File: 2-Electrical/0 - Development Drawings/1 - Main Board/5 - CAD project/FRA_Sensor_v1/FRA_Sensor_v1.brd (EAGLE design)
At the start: 79 x 94 mm, 144 parts, among them IC1 CP2101, IC2 LMV611, J1 FTDI, J3 USB, T1 BC847, T2 BC847, T3 BC847, U1 DS1307Z, U2 ESP-WROOM-32, U3 CH340G, U4 W25Q32FV, U6 MMA8452QL, Y1 12MHz, Y2 32.768kHz, Y3 32.768kHz, Y4 12MHz

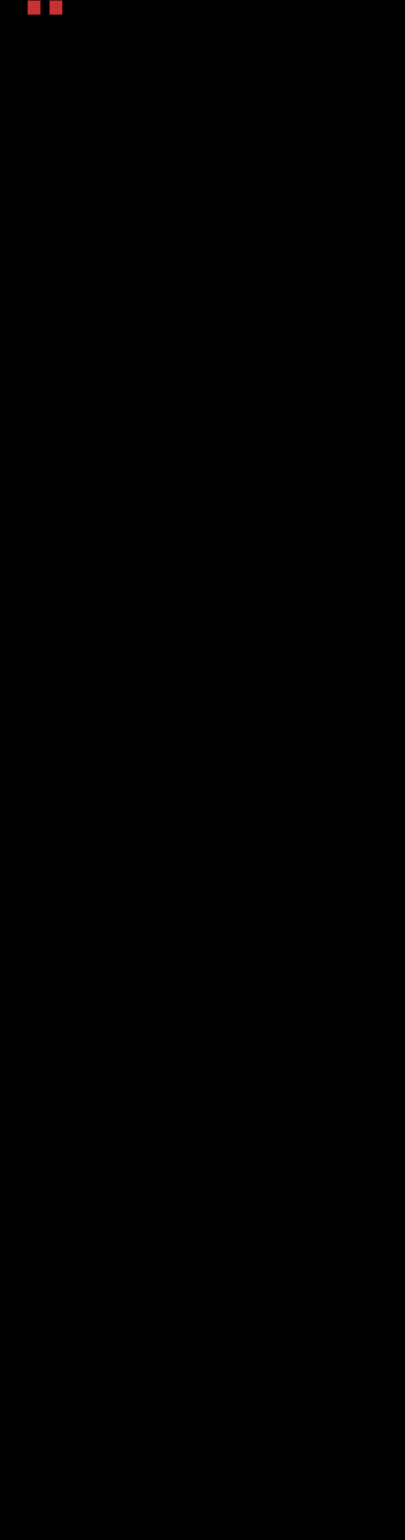
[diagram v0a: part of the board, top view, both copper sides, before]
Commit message: TGS2611 integration
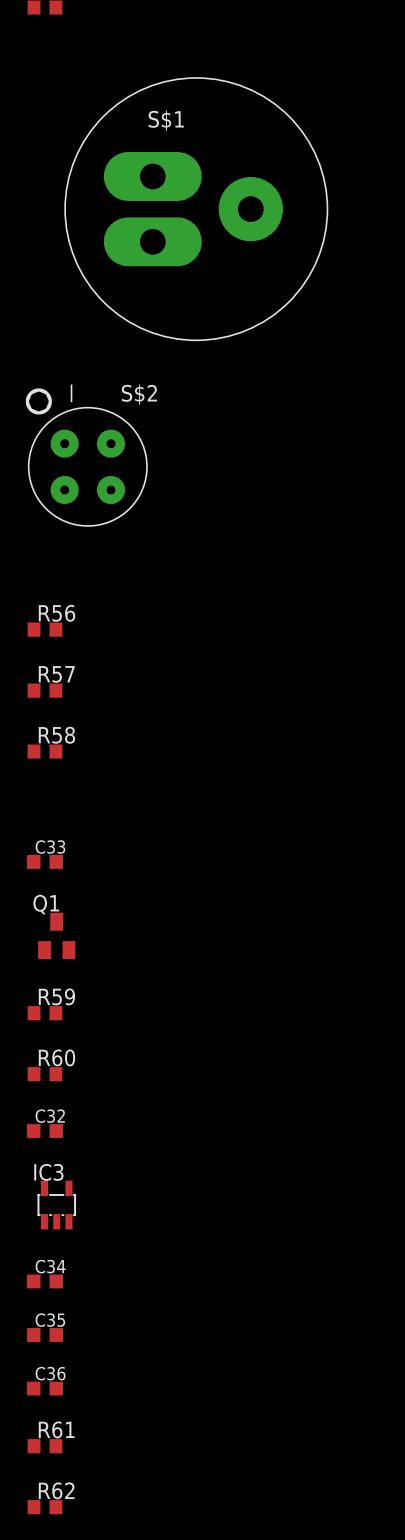
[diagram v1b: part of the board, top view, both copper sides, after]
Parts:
- added C32, C33, C34: 100n, resistor:C0603K
- added C35, C36: 1u, resistor:C0603K
- added IC3: TS520533, v-reg:SOT25
- added Q1: Si2300DS, adafruit:SOT23
- added R56: 5.1k, resistor:R0603
- added R57: 0R, resistor:R0603
- added R58, R60, R61, R62: (DNI), resistor:R0603
- added R59: 1M, resistor:R0603
- added S$1: CITIPEL_4P50, FRA_eagle_lib:TH3_4P50
- added S$2: FIGARO_2611, FRA_eagle_lib:TH4_TGS2611
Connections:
- new net 3V3_TGS2611: C36.1, IC3.5, R61.2
- new net ADC_TGS2611: C33.1, R57.2, R58.2
- new net N$53: Q1.3, S$2.1
- new net N$56: C34.1, IC3.4
- new net RS_NEG: R56.1, R57.1, S$2.2
- new net RS_POS: C32.1, R60.2, R61.1, R62.1, S$2.3
- new net TGS2611_HEAT_EN: Q1.1, R59.1
- new net VREF_TGS6211: R62.2
- new net V_NEG: S$1.V_NEG
- new net V_POS: S$1.V_POS
- net 5V: now also C35.1, IC3.1, IC3.3, R60.1, S$2.4
- net GND: now also C32.2, C33.2, C34.2, C35.2, C36.2, IC3.2, Q1.2, R56.2, R58.1, R59.2
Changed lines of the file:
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@@
 <element name="DRILEGEND" library="drilegend" package="DRILEGEND" value="" x="-0.2032" y="-6.332271875"/>
 <element name="R47" library="resistor" package="R0603" value="470k" x="-17.966465625" y="-32.130203125"/>
+<element name="S$1" library="FRA_eagle_lib" package="TH3_4P50" value="CITIPEL_4P50" x="-6.201365625" y="-47.806703125"/>
+<element name="S$2" library="FRA_eagle_lib" package="TH4_TGS2611" value="FIGARO_2611" x="-14.63435625" y="-67.843534375"/>
+<element name="R56" library="resistor" package="R0603" value="5.1k" x="-17.966465625" y="-80.501196875"/>
+<element name="R57" library="resistor" package="R0603" value="0R" x="-17.966465625" y="-85.242528125"/>
+<element name="R58" library="resistor" package="R0603" value="(DNI)" x="-17.966465625" y="-89.983859375"/>
+<element name="C33" library="resistor" package="C0603K" value="100n" x="-17.963265625" y="-98.564190625"/>
+<element name="Q1" library="adafruit" package="SOT23" value="Si2300DS" x="-17.051865625" y="-104.320521875"/>
+<element name="R59" library="resistor" package="R0603" value="1M" x="-17.966465625" y="-110.331853125"/>
+<element name="R60" library="resistor" package="R0603" value="(DNI)" x="-17.966465625" y="-115.073184375"/>
+<element name="C32" library="resistor" package="C0603K" value="100n" x="-17.963265625" y="-119.49085"/>
+<element name="IC3" library="v-reg" package="SOT25" value="TS520533" x="-17.051865625" y="-125.24718125"/>
+<element name="C34" library="resistor" package="C0603K" value="100n" x="-17.963265625" y="-131.188846875"/>
+<element name="C35" library="resistor" package="C0603K" value="1u" x="-17.963265625" y="-135.3515125"/>
+<element name="C36" library="resistor" package="C0603K" value="1u" x="-17.963265625" y="-139.514178125"/>
+<element name="R61" library="resistor" package="R0603" value="(DNI)" x="-17.966465625" y="-144.000509375"/>
+<element name="R62" library="resistor" package="R0603" value="(DNI)" x="-17.966465625" y="-148.741840625"/>
 </elements>
 <signals>
@@
 <wire x1="63.1825" y1="18.0975" x2="63.8175" y2="18.0975" width="0.3048" layer="1"/>
 <contactref element="TP30" pad="TP"/>
+<contactref element="C33" pad="2"/>
+<contactref element="R58" pad="1"/>
+<contactref element="R56" pad="2"/>
+<contactref element="Q1" pad="2"/>
+<contactref element="R59" pad="2"/>
+<contactref element="C32" pad="2"/>
+<contactref element="IC3" pad="2"/>
+<contactref element="C34" pad="2"/>
+<contactref element="C35" pad="2"/>
+<contactref element="C36" pad="2"/>
+<wire x1="-17.088265625" y1="-135.3515125" x2="-17.088265625" y2="-139.514178125" width="0" layer="19" extent="1-1"/>
+<wire x1="-17.088265625" y1="-131.188846875" x2="-17.088265625" y2="-135.3515125" width="0" layer="19" extent="1-1"/>
+<wire x1="-17.051865625" y1="-126.54718125" x2="-17.088265625" y2="-131.188846875" width="0" layer="19" extent="1-1"/>
+<wire x1="-17.088265625" y1="-119.49085" x2="-17.051865625" y2="-126.54718125" width="0" layer="19" extent="1-1"/>
+<wire x1="-17.116465625" y1="-110.331853125" x2="-17.088265625" y2="-119.49085" width="0" layer="19" extent="1-1"/>
+<wire x1="-16.101865625" y1="-105.420521875" x2="-17.116465625" y2="-110.331853125" width="0" layer="19" extent="1-1"/>
+<wire x1="-17.088265625" y1="-98.564190625" x2="-16.101865625" y2="-105.420521875" width="0" layer="19" extent="1-1"/>
+<wire x1="-18.816465625" y1="-89.983859375" x2="-17.088265625" y2="-98.564190625" width="0" layer="19" extent="1-1"/>
+<wire x1="-17.116465625" y1="-80.501196875" x2="-18.816465625" y2="-89.983859375" width="0" layer="19" extent="1-1"/>
+<wire x1="24.765" y1="1.905" x2="-17.116465625" y2="-80.501196875" width="0" layer="19" extent="1-16"/>
+<wire x1="63.1825" y1="18.0975" x2="63.1825" y2="18.185" width="0" layer="19" extent="1-1"/>
+<wire x1="27.94" y1="34.29" x2="28.2575" y2="33.9725" width="0" layer="19" extent="16-16"/>
+<wire x1="29.5275" y1="36.195" x2="28.2575" y2="36.195" width="0" layer="19" extent="16-16"/>
+<wire x1="13.97" y1="7.835" x2="15.025" y2="8.89" width="0" layer="19" extent="1-1"/>
+<wire x1="45.085" y1="1.5875" x2="44.87" y2="3.4925" width="0" layer="19" extent="1-1"/>
+<wire x1="13.97" y1="10.4775" x2="15.025" y2="8.89" width="0" layer="19" extent="1-1"/>
+<wire x1="5.715" y1="54.37" x2="5.715" y2="54.2925" width="0" layer="19" extent="16-16"/>
+<wire x1="52.07" y1="55.245" x2="46.99" y2="51.435" width="0" layer="19" extent="1-1"/>
+<wire x1="54.9275" y1="45.4025" x2="46.99" y2="49.9237" width="0" layer="19" extent="1-1"/>
+<wire x1="63.1825" y1="50.165" x2="54.9275" y2="45.4025" width="0" layer="19" extent="1-1"/>
+<wire x1="69.5325" y1="49.2125" x2="63.1825" y2="50.165" width="0" layer="19" extent="1-1"/>
+<wire x1="69.5325" y1="46.355" x2="69.5325" y2="49.2125" width="0" layer="19" extent="1-1"/>
+<wire x1="75.2475" y1="13.0175" x2="63.6025" y2="13.97" width="0" layer="19" extent="1-1"/>
 </signal>
 <signal name="5V">
@@
 <wire x1="26.67" y1="4.1275" x2="26.67" y2="2.54" width="0.3048" layer="1"/>
 <wire x1="29.21" y1="2.54" x2="29.21" y2="4.1275" width="0.3048" layer="1"/>
+<contactref element="S$2" pad="4"/>
+<contactref element="R60" pad="1"/>
+<contactref element="IC3" pad="1"/>
+<contactref element="IC3" pad="3"/>
+<contactref element="C35" pad="1"/>
+<wire x1="-18.001865625" y1="-126.54718125" x2="-18.838265625" y2="-135.3515125" width="0" layer="19" extent="1-1"/>
+<wire x1="-16.101865625" y1="-126.54718125" x2="-18.001865625" y2="-126.54718125" width="0" layer="19" extent="1-1"/>
+<wire x1="-18.816465625" y1="-115.073184375" x2="-18.001865625" y2="-126.54718125" width="0" layer="19" extent="1-1"/>
+<wire x1="-12.83435625" y1="-66.043534375" x2="-18.816465625" y2="-115.073184375" width="0" layer="19" extent="1-1"/>
+<wire x1="26.67" y1="2.54" x2="-12.83435625" y2="-66.043534375" width="0" layer="19" extent="1-1"/>
+<wire x1="26.67" y1="6.0325" x2="26.67" y2="4.1275" width="0" layer="19" extent="1-1"/>
+<wire x1="26.035" y1="7.62" x2="26.67" y2="6.0325" width="0" layer="19" extent="16-16"/>
+<wire x1="28.575" y1="5.3975" x2="28.575" y2="5.3975" width="0" layer="19" extent="1-16"/>
+<wire x1="30.7975" y1="5.3975" x2="30.1625" y2="5.715" width="0" layer="19" extent="1-1"/>
+<wire x1="31.75" y1="4.1275" x2="31.75" y2="4.445" width="0" layer="19" extent="1-1"/>
+<wire x1="31.75" y1="6.0325" x2="31.4325" y2="5.715" width="0" layer="19" extent="1-1"/>
+<wire x1="29.21" y1="6.0325" x2="29.5275" y2="5.3975" width="0" layer="19" extent="16-16"/>
+<wire x1="29.21" y1="4.1275" x2="29.5275" y2="5.3975" width="0" layer="19" extent="16-16"/>
 </signal>
 <signal name="RXD0_CP2101IN">
@@
 <wire x1="71.755" y1="34.7675" x2="71.2775" y2="34.29" width="0.3048" layer="1"/>
 </signal>
+<signal name="V_NEG">
+<contactref element="S$1" pad="V_NEG"/>
+</signal>
+<signal name="V_POS">
+<contactref element="S$1" pad="V_POS"/>
+</signal>
+<signal name="RS_NEG">
+<contactref element="S$2" pad="2"/>
+<contactref element="R56" pad="1"/>
+<contactref element="R57" pad="1"/>
+<wire x1="-18.816465625" y1="-80.501196875" x2="-18.816465625" y2="-85.242528125" width="0" layer="19" extent="1-1"/>
+<wire x1="-16.43435625" y1="-69.643534375" x2="-18.816465625" y2="-80.501196875" width="0" layer="19" extent="1-1"/>
+</signal>
+<signal name="ADC_TGS2611">
+<contactref element="R57" pad="2"/>
+<contactref element="R58" pad="2"/>
+<contactref element="C33" pad="1"/>
+<wire x1="-17.116465625" y1="-89.983859375" x2="-18.838265625" y2="-98.564190625" width="0" layer="19" extent="1-1"/>
+<wire x1="-17.116465625" y1="-85.242528125" x2="-17.116465625" y2="-89.983859375" width="0" layer="19" extent="1-1"/>
+</signal>
+<signal name="N$53">
+<contactref element="S$2" pad="1"/>
+<contactref element="Q1" pad="3"/>
+<wire x1="-16.43435625" y1="-66.043534375" x2="-17.051865625" y2="-103.220521875" width="0" layer="19" extent="1-1"/>
+</signal>
+<signal name="TGS2611_HEAT_EN">
+<contactref element="Q1" pad="1"/>
+<contactref element="R59" pad="1"/>
+<wire x1="-18.001865625" y1="-105.420521875" x2="-18.816465625" y2="-110.331853125" width="0" layer="19" extent="1-1"/>
+</signal>
+<signal name="RS_POS">
+<contactref element="S$2" pad="3"/>
+<contactref element="R60" pad="2"/>
+<contactref element="C32" pad="1"/>
+<contactref element="R61" pad="1"/>
+<contactref element="R62" pad="1"/>
+<wire x1="-18.816465625" y1="-144.000509375" x2="-18.816465625" y2="-148.741840625" width="0" layer="19" extent="1-1"/>
+<wire x1="-18.838265625" y1="-119.49085" x2="-18.816465625" y2="-144.000509375" width="0" layer="19" extent="1-1"/>
+<wire x1="-17.116465625" y1="-115.073184375" x2="-18.838265625" y2="-119.49085" width="0" layer="19" extent="1-1"/>
+<wire x1="-12.83435625" y1="-69.643534375" x2="-17.116465625" y2="-115.073184375" width="0" layer="19" extent="1-1"/>
+</signal>
+<signal name="N$56">
+<contactref element="IC3" pad="4"/>
+<contactref element="C34" pad="1"/>
+<wire x1="-16.101865625" y1="-123.94718125" x2="-18.838265625" y2="-131.188846875" width="0" layer="19" extent="1-1"/>
+</signal>
+<signal name="3V3_TGS2611">
+<contactref element="C36" pad="1"/>
+<contactref element="IC3" pad="5"/>
+<contactref element="R61" pad="2"/>
+<wire x1="-18.838265625" y1="-139.514178125" x2="-17.116465625" y2="-144.000509375" width="0" layer="19" extent="1-1"/>
+<wire x1="-18.001865625" y1="-123.94718125" x2="-18.838265625" y2="-139.514178125" width="0" layer="19" extent="1-1"/>
+</signal>
+<signal name="VREF_TGS6211">
+<contactref element="R62" pad="2"/>
+</signal>
 </signals>

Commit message: programming interface ready
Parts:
- removed C11, C12: 10u, resistor:C0603K
- removed C13: 100n, resistor:C0603K
- removed C14, C15: 220u, resistor:153CLV-0605
- removed C7, C8: 22p, resistor:C0402
- removed D4: BAS17, nxp_60:SOT23
- removed LED_24: LED_ring_24, pinhead:1X04
- removed LS1: BUZZER-PTH_KIT_NO_SILK, SparkFun-Electromechanical:BUZZER-12MM-NS-KIT
- removed R26, R28, R30: 12k, resistor:R0603
- removed R27, R29: 2k2, resistor:R0603
- removed R32: 100, resistor:R0603
- removed R47: 470k, resistor:R0603
- removed R48, R50, R51, R55: 0, resistor:R0603
- removed R49, R52, R53: 0(NC), resistor:R0603
- removed SJR1: ESP12E/F, esp12e:ESP8266-ESP12E
- removed TP1, TP10, TP12, TP14, TP15, TP16, TP17, TP2, TP24, TP25, TP26, TP27, TP3, TP4, TP6, TP9: TPTP10R, testpad:TP10R
- removed U3: CH340G, SparkFun-IC-Comms:SO016
- removed U6: MMA8452QL, MMA8452Q:QFN-16_0.5MM-EXTRA
- removed Y1: 12MHz, SparkFun-Clocks:HC49UP
- removed Y4: 12MHz, SparkFun-Clocks:CRYSTAL-SMD-3.2X1.5MM
- added D2: PESD1CAN, diode:SOT23
- added JTAG1: (no value), microbuilder:2X05_1.27MM_SMT
- added U$2: HEADER_3X6P_ESPPROG, FRA_eagle_lib:2X03_1.27MM_SMT
- C16: value 470p -> 1n
- D1: value WS2812B -> PESD1CAN; device SparkFun-LED:WS2812B -> diode:SOT23
- R10: value 470 -> 100
- R12, R13, R24: value 0 -> 100
- R23: value 0 -> 5k(DNI)
- R7: value 470 -> 0
- R9: value 0 -> 100k
- moved R24 300.7 mm to (-26.7, -217.2), flipped to the top, turned to 0 degrees
- moved R13 255.7 mm to (-26.7, -212.1), flipped to the top, turned to 0 degrees
- moved R12 252.1 mm to (-26.7, -207.0), flipped to the top, turned to 0 degrees
- moved R10 233.8 mm to (-26.7, -201.9), flipped to the top, turned to 0 degrees
- moved R9 219.0 mm to (-26.7, -196.8), flipped to the top, turned to 0 degrees
- moved R7 217.1 mm to (-26.7, -186.7), flipped to the top, turned to 0 degrees
- moved R8 214.9 mm to (-26.7, -191.8), flipped to the top, turned to 0 degrees
- moved D1 214.1 mm to (-17.1, -159.5), flipped to the top
- moved R23 212.4 mm to (-18.0, -153.5), flipped to the top, turned to 0 degrees
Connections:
- removed net EN: R26.1, SJR1.3
- removed net GPIO15: R30.1, SJR1.10
- removed net GPIO16: SJR1.4, TP1.TP
- removed net GPIO2: R28.1, SJR1.11, U2.24
- removed net GPIO5: R13.1, SJR1.14, TP2.TP
- removed net INT1: SJR1.7, TP4.TP, U2.10, U6.11
- removed net INT2: U2.11, U6.9
- removed net LED_12DI: LED_12.1, R24.1
- removed net LED_24_DI: LED_24.1, R23.1
- removed net LED_24_DO: LED_24.4, R24.2
- removed net LED_WS: D1.4, R51.1, R52.1, SJR1.6
- removed net N$10: C8.1, U3.8, Y1.2, Y4.P$2
- removed net N$15: D4.3, U3.16
- removed net N$20: R48.2, R49.2, U2.23
- removed net N$21: R31.1, SJR1.5, TP3.TP
- removed net N$23: R51.2, U2.33
- removed net N$24: R52.2, U2.36
- removed net N$25: LS1.-, R38.1, R47.1, T3.3
- removed net N$33: C20.1, LS1.+, R32.2, R47.2
- removed net N$41: R50.2, U2.29
- removed net N$42: R53.2, U2.37
- removed net N$43: TP14.TP, U2.7
- removed net N$44: TP15.TP, U2.6
- removed net N$45: TP16.TP, U2.5
- removed net N$46: TP17.TP, U2.26
- removed net N$63: TP10.TP, U2.14
- removed net N$64: TP12.TP, U2.16
- removed net N$65: TP24.TP, U2.13
- removed net N$66: TP25.TP, U2.27
- removed net N$67: TP26.TP, U2.28
- removed net N$68: TP27.TP, U2.25
- removed net N$9: C13.1, U3.4
- new net MTCK: R13.2, U2.16
- new net MTDI: R10.2, R9.1, U2.14
- new net MTDO: R12.2, U2.23
- new net MTMS: R24.2, U2.13
- new net N$17: R38.1
- new net V_USB: J3.VBUS, R43.2
- net 3.3V: now also R23.1, R7.1, R8.2; no longer C11.1, C12.1, R26.2, R27.2, R28.2, R29.2, SJR1.8, U6.1, U6.14
- net 5V: no longer C14.+, C15.+, D4.1, J3.VBUS, LED_12.2, LED_24.2, R32.1, R43.2
- net ADC: no longer SJR1.2, U2.4
- net DTR: no longer U3.13
- net D_N: no longer R9.1
- net D_P: no longer R8.1
- net FLASH_CS: no longer R49.1, R50.1
- net GND: now also JTAG1.3, JTAG1.5, JTAG1.7, JTAG1.9, R9.2, U$2.4; no longer C11.2, C12.2, C13.2, C14.-, C15.-, C7.2, C8.2, D1.3, LED_12.3, LED_24.3, R30.2, SJR1.9, U3.1, U6.10, U6.12, U6.5
- net GPIO0: now also R23.2, U$2.6, U2.25; no longer R55.1
- net MISO: no longer SJR1.18
- net MOSI: no longer SJR1.21
- net N$18: now also JTAG1.8, R10.1; no longer D1.2, R23.2
- net N$19: no longer U6.2
- net N$22: no longer SJR1.17
- net N$3: no longer D1.1
- net N$4: now also JTAG1.6, R12.1; no longer R7.1, U3.2
- net N$40: no longer U6.7
- net N$5: now also JTAG1.2, R24.1; no longer R10.1, U3.3
- net N$6: now also R7.2, U$2.2; no longer R8.2, U3.5
- net N$7: now also JTAG1.4, R13.1; no longer R9.2, U3.6
- net N$8: now also JTAG1.1, R8.1; no longer C7.1, U3.7, Y1.1, Y4.P$1
- net NRST: no longer SJR1.1
- net PWM: no longer R12.2, R13.2, R48.1, R53.1
- net RTS: no longer U3.14
- net RXD0: no longer R12.1, R7.2, SJR1.15
- net SCL: no longer R27.1, R55.2, SJR1.12, TP6.TP, U6.4
- net SCLK: no longer SJR1.22
- net SDA: no longer R29.1, SJR1.13, TP9.TP, U6.6
- net SPI_HOLD: no longer SJR1.19
- net SPI_WP: no longer SJR1.20
- net TXD0: no longer R10.2, SJR1.16
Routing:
- net INT1: track 132.7 -> 0.00 mm, vias 2 -> 0
- net INT2: track 76.5 -> 0.00 mm
- net LED_24_DI: track 56.1 -> 0.00 mm
- net GND: track 630.3 -> 577.7 mm
- net GPIO2: track 52.3 -> 0.00 mm, vias 2 -> 0
- net LED_WS: track 50.1 -> 0.00 mm, vias 1 -> 0
- net 5V: track 232.8 -> 194.0 mm
- net SDA: track 180.1 -> 151.4 mm, vias 8 -> 7
- net 3.3V: track 397.8 -> 370.3 mm, vias 28 -> 27
- net SCL: track 169.3 -> 147.5 mm, vias 6 -> 5
- net PWM: track 138.0 -> 118.3 mm
- net N$8: track 15.0 -> 0.00 mm
- net NRST: track 87.0 -> 72.9 mm
- net N$10: track 13.4 -> 0.00 mm
- net LED_24_DO: track 10.6 -> 0.00 mm
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
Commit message: SCH update
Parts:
- removed C17: 100n, resistor:C0603K
- removed R17, R31: 0, resistor:R0603
- removed R54: 47k, resistor:R0603
- removed TP18, TP19, TP20, TP21, TP22, TP23, TP5, TP8: TPTP10R, testpad:TP10R
- removed U4: W25Q32FV, SparkFun-IC-Memory:SOIC-8
- added U$3: MICROSD, adafruit:MICROSD
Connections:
- removed net FLASH_CS: R17.2, R31.2, U4.1
- removed net MISO: R54.1, U4.2
- removed net MOSI: TP5.TP, U4.5
- removed net N$22: R17.1
- removed net N$47: TP18.TP, U2.17
- removed net N$48: TP19.TP, U2.18
- removed net N$49: TP20.TP, U2.19
- removed net N$50: TP21.TP, U2.20
- removed net N$51: TP22.TP, U2.21
- removed net N$52: TP23.TP, U2.22
- removed net SCLK: U4.6
- removed net SPI_WP: TP8.TP, U4.3
- new net VSPI_CS_ETH: U2.37
- new net VSPI_MISO: U2.31
- new net VSPI_MOSI: U2.30
- new net VSPI_SCK: U2.29
- net 3.3V: no longer C17.1, R54.2, U4.8
- net GND: no longer C17.2, U4.4
- net SCL: now also U2.36; no longer U2.31
- net SDA: now also U2.33; no longer U2.30
- net SPI_HOLD: no longer U4.7
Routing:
- net FLASH_CS: track 46.0 -> 0.00 mm, vias 3 -> 0
- net NRST: track 72.9 -> 36.5 mm, vias 4 -> 2
- net SCL: track 147.5 -> 113.2 mm, vias 5 -> 4
- net SPI_WP: track 32.4 -> 0.00 mm, vias 2 -> 0
- net SCLK: track 31.0 -> 0.00 mm, vias 2 -> 0
- net MISO: track 27.9 -> 0.00 mm, vias 2 -> 0
- net SDA: track 151.4 -> 123.7 mm, vias 7 -> 4
- net MOSI: track 27.4 -> 0.00 mm, vias 2 -> 0
- net N$22: track 26.7 -> 0.00 mm, vias 2 -> 0
- net 3.3V: track 370.3 -> 357.0 mm
- net GND: track 577.7 -> 571.7 mm
- net N$51: track 3.32 -> 0.00 mm
- net N$49: track 3.32 -> 0.00 mm
- net N$47: track 3.32 -> 0.00 mm
- net N$52: track 2.05 -> 0.00 mm
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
